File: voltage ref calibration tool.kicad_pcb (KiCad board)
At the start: 2 copper layers, 148.8 x 79.5 mm, 69 parts, among them J1 AudioJack2_SwitchT, J2 Molex-MicroFit_43650-0316, J3 AudioJack2_SwitchT, J4 Conn_01x02, J5 Conn_01x02, SW1 SW_SP6T, SW2 B3F-1020, SW3 B3F-1020, SW4 B3F-1020, SW5 B3F-1020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

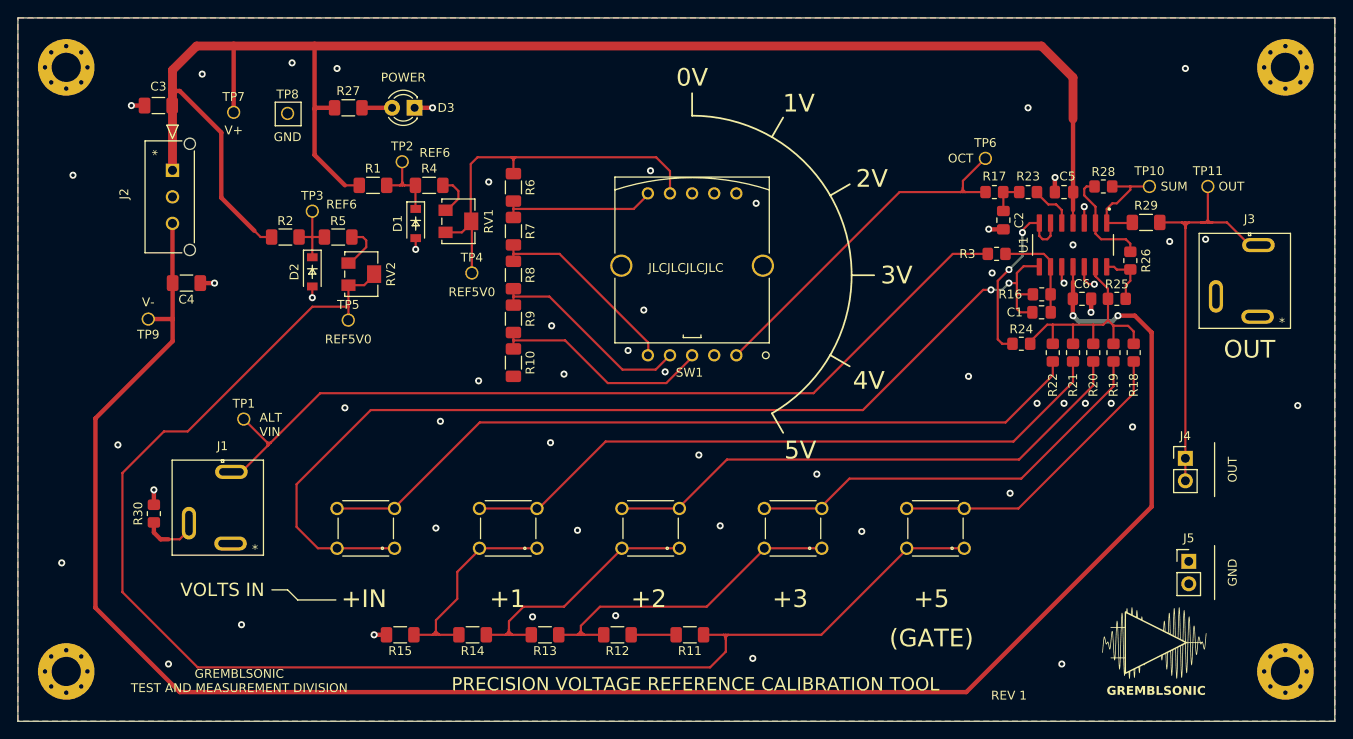
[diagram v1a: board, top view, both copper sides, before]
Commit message: don't invert alt ref in
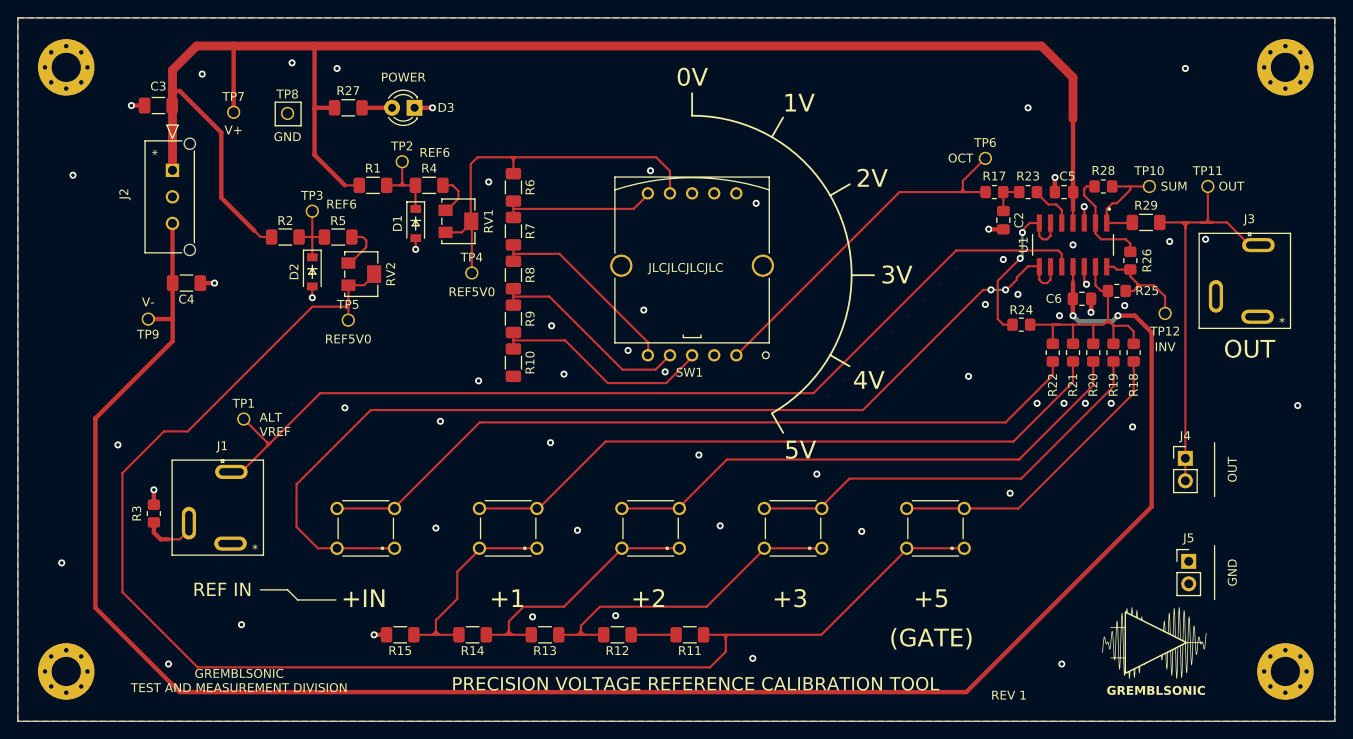
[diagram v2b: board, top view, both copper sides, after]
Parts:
- removed C1: 33pF, Capacitor_SMD:C_0805_2012Metric_Pad1.18x1.45mm_HandSolder
- removed R16: 100k 0.1%, Resistor_SMD:R_0805_2012Metric_Pad1.20x1.40mm_HandSolder
- removed R30: 2k2, Resistor_SMD:R_0805_2012Metric_Pad1.20x1.40mm_HandSolder
- added TP12: TP, Aaron_Pads:TP_HeaderPin_P2.54mm_round, F.Cu at (166.0, 66.4)
- R3: value 100k 0.1% -> 10k
- moved R3 99.7 mm to (51.7, 89.0), turned to -90 degrees
- moved R24 2.16 mm to (149.7, 67.7)
- moved R25 0.89 mm to (160.5, 63.9)
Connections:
- R3 pad 1: /ALT_V_IN -> GND
- R3 pad 2: Net-(U1C--) -> Net-(J1-PadTN)
- SW6 pad 1: /ALT_INV -> /ALT_BUF
- U1 pad 10: GND -> /ALT_V_IN
- U1 pad 8: /ALT_INV -> /ALT_BUF
- U1 pad 9: Net-(U1C--) -> /ALT_BUF
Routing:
- net /ALT_INV: track 118.4 -> 0.00 mm, vias 2 -> 0
- net /ALT_BUF: track 0.00 -> 115.7 mm, vias 0 -> 2
- net Net-(U1C--): track 10.2 -> 0.00 mm
- net /ALT_V_IN: track 99.5 -> 109.5 mm
- net /VINV: track 5.95 -> 13.1 mm
- net GND: track 22.2 -> 19.5 mm, vias 57 -> 60
- net Net-(U1B--): track 22.0 -> 19.9 mm
- net /VGND: track 29.0 -> 30.8 mm
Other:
- board text added: "ALT VREF"
- board text added: "INV"
- board text added: "REF IN"
- board text removed: "ALT VIN"
- board text removed: "VOLTS IN"

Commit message: Some final cleanup. Ready to go.
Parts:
- added R16: 47k, Resistor_SMD:R_0805_2012Metric_Pad1.20x1.40mm_HandSolder, F.Cu at (155.6, 66.4)
- added R30: 47k, Resistor_SMD:R_0805_2012Metric_Pad1.20x1.40mm_HandSolder, F.Cu at (157.4, 49.8)
- added R31: 10k, Resistor_SMD:R_0805_2012Metric_Pad1.20x1.40mm_HandSolder, F.Cu at (176.4, 74.4)
- moved TP5 58.1 mm to (118.4, 104.3)
- moved TP4 16.4 mm to (94.7, 47.1)
- moved TP10 2.62 mm to (163.2, 49.7)
- moved TP8 2.41 mm to (67.6, 41.5)
- moved C6 2.22 mm to (154.6, 63.9), turned to 180 degrees
- moved TP7 2.16 mm to (60.7, 41.5)
- moved G*** 2.00 mm to (162.7, 103.5)
- moved H2 2.00 mm to (177.6, 38.6)
- moved H4 2.00 mm to (177.6, 106.9)
- moved R28 1.65 mm to (160.5, 52.7)
- moved D1 1.57 mm to (79.8, 55.9)
- moved J5 1.28 mm to (168.3, 93.2)
- moved R25 0.65 mm to (161.2, 63.8)
- moved R24 0.38 mm to (149.7, 68.1)
- turned RV1 to 0 degrees
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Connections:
- J3 pad S: GND -> Net-(J3-PadS)
- RV1 pad 1: Net-(R4-Pad2) -> /REF5V0A
- RV1 pad 3: /REF5V0A -> Net-(R4-Pad2)
- RV2 pad 1: Net-(R5-Pad2) -> /REF5V0B
- RV2 pad 3: /REF5V0B -> Net-(R5-Pad2)
- U1 pad 12: GND -> Net-(U1D-+)
- U1 pad 3: GND -> Net-(U1A-+)
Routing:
- net Vcc+: track 183.1 -> 191.2 mm
- net Net-(U1D-+): track 0.00 -> 6.94 mm
- net Net-(J3-PadS): track 0.00 -> 6.48 mm
- net Net-(U1A-+): track 0.00 -> 5.63 mm
- net /REF5V0A: track 43.0 -> 38.9 mm
- net Net-(J1-PadTN): track 5.28 -> 8.94 mm
- net /VGND: track 30.8 -> 33.7 mm
- net /OUT: track 47.0 -> 49.6 mm
- net /REF5V0B: track 161.1 -> 163.1 mm
- net /ALT_V_IN: track 109.5 -> 111.5 mm
- net /VSUM: track 12.7 -> 14.3 mm
- net /REF6B: track 7.98 -> 9.41 mm
- net /OctaveSelect: track 41.5 -> 42.9 mm
- net Net-(U1B-+): track 4.51 -> 5.70 mm
- net Net-(U1A--): track 12.0 -> 11.1 mm
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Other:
- board size 148.8 x 79.5 mm -> 147.1 x 79.5 mm
- board text added: "+12V"
- board text added: "-12V"
- board text added: "1"
